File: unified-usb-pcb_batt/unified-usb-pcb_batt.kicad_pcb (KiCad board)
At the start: 2 copper layers, 30 x 34 mm, 39 parts, among them J1 QI, J2 USB_C_Receptacle_USB2.0, J3 USB_Out, J4 BATT, J5 THERM, SW1 SW_SPDT, U1 SRV05-4, U2 DW01A, U3 TP4056, U4 FS8205

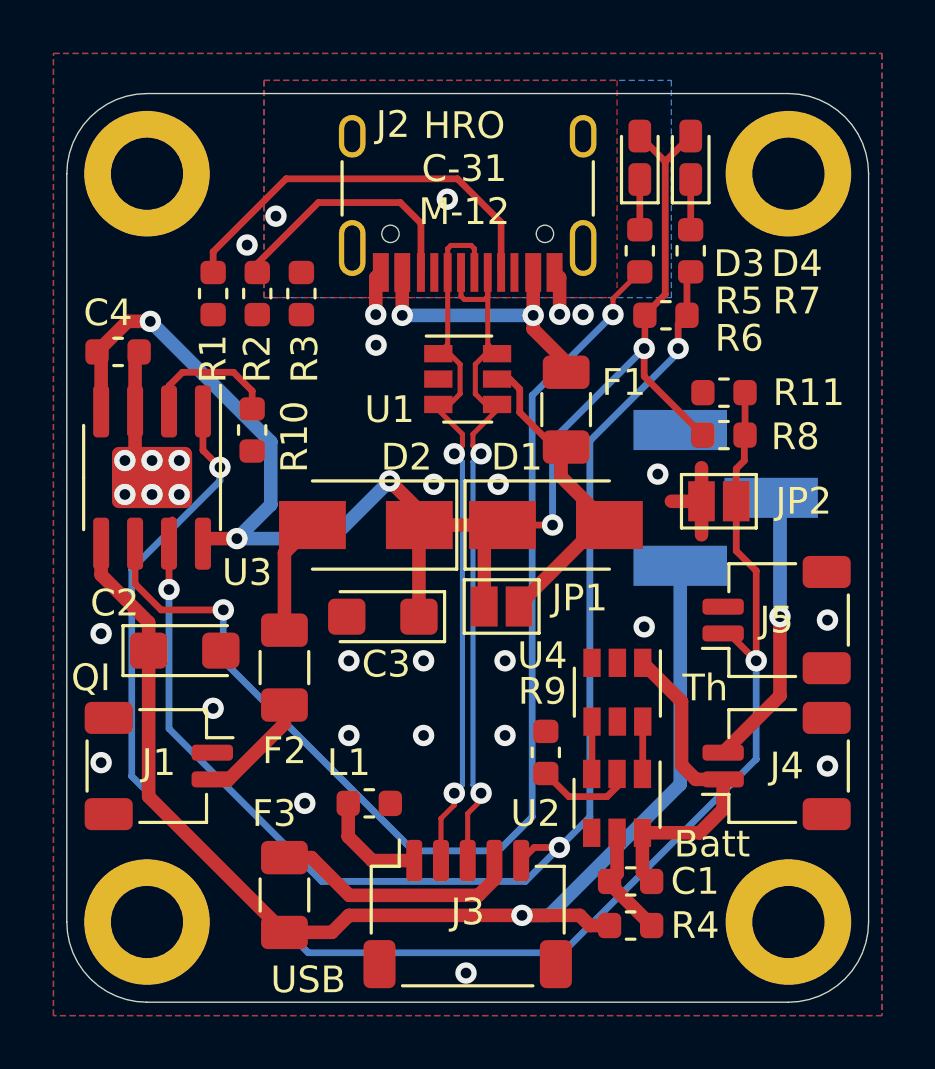
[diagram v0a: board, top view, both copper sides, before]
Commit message: fixed batt schem, added readme warning about broken pcb
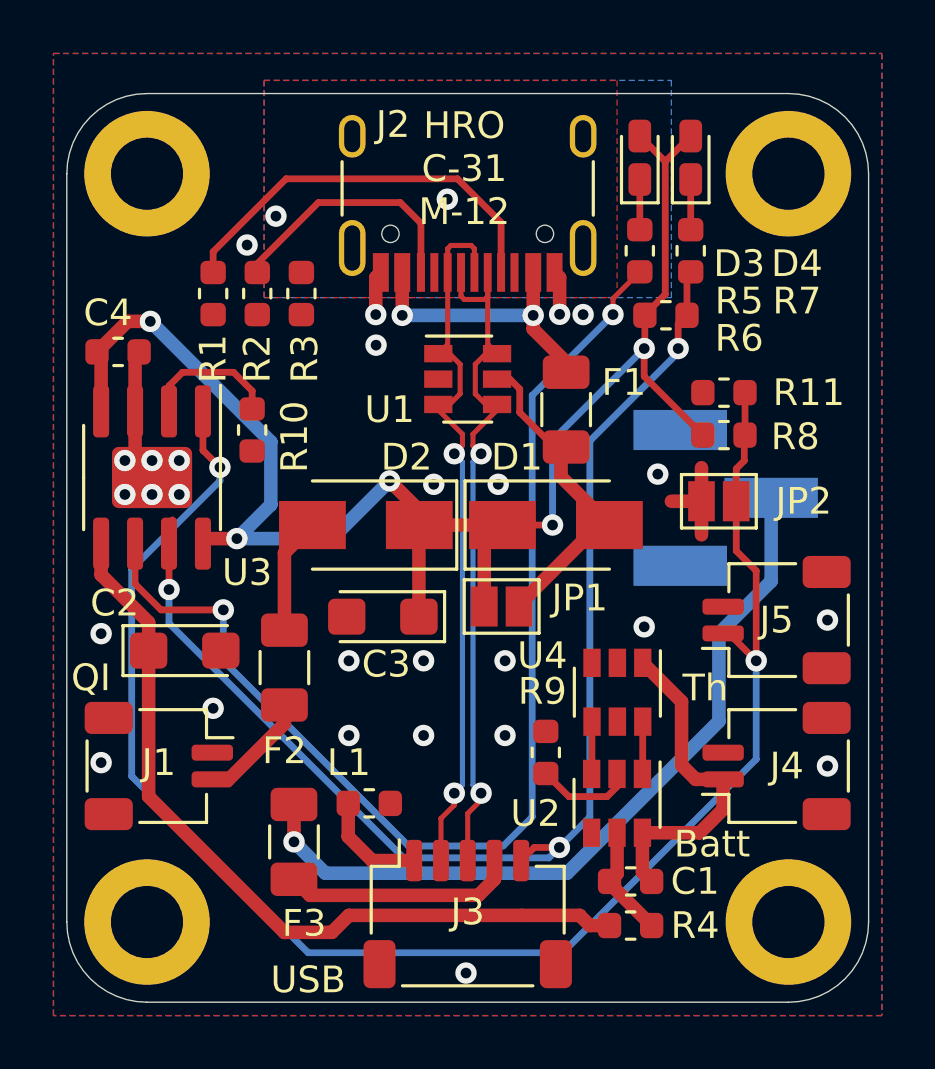
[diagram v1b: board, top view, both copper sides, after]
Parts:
- moved F3 2.02 mm to (24.3, 47.3), turned to 90 degrees
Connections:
- C2 pad 1: VOUT -> Net-(C2-Pad1)
- J4 pad 2: Net-(J4-Pad2) -> Net-(C2-Pad1)
- R4 pad 2: VOUT -> Net-(C2-Pad1)
- SW1 pad 1: Net-(SW1-Pad1) -> +5V
- SW1 pad 2: Net-(J4-Pad2) -> VOUT
- SW1 pad 3: VOUT -> Net-(C2-Pad1)
- U3 pad 5: VOUT -> Net-(C2-Pad1)
- U3 pad 9: GNDPWR -> (no net)
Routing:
- net Net-(C2-Pad1): track 0.00 -> 30.0 mm
- net VOUT: track 46.1 -> 30.0 mm
- net Net-(J4-Pad2): track 11.2 -> 0.00 mm, vias 1 -> 0
- net chgsense: track 49.7 -> 46.6 mm
- net Net-(F3-Pad1): track 9.39 -> 8.70 mm
- net GNDPWR: vias 28 -> 27

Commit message: slight rev bump - fixed battery pcb, re-exported new prod files for jlcpcb. Probably last commit, project no longer in active development
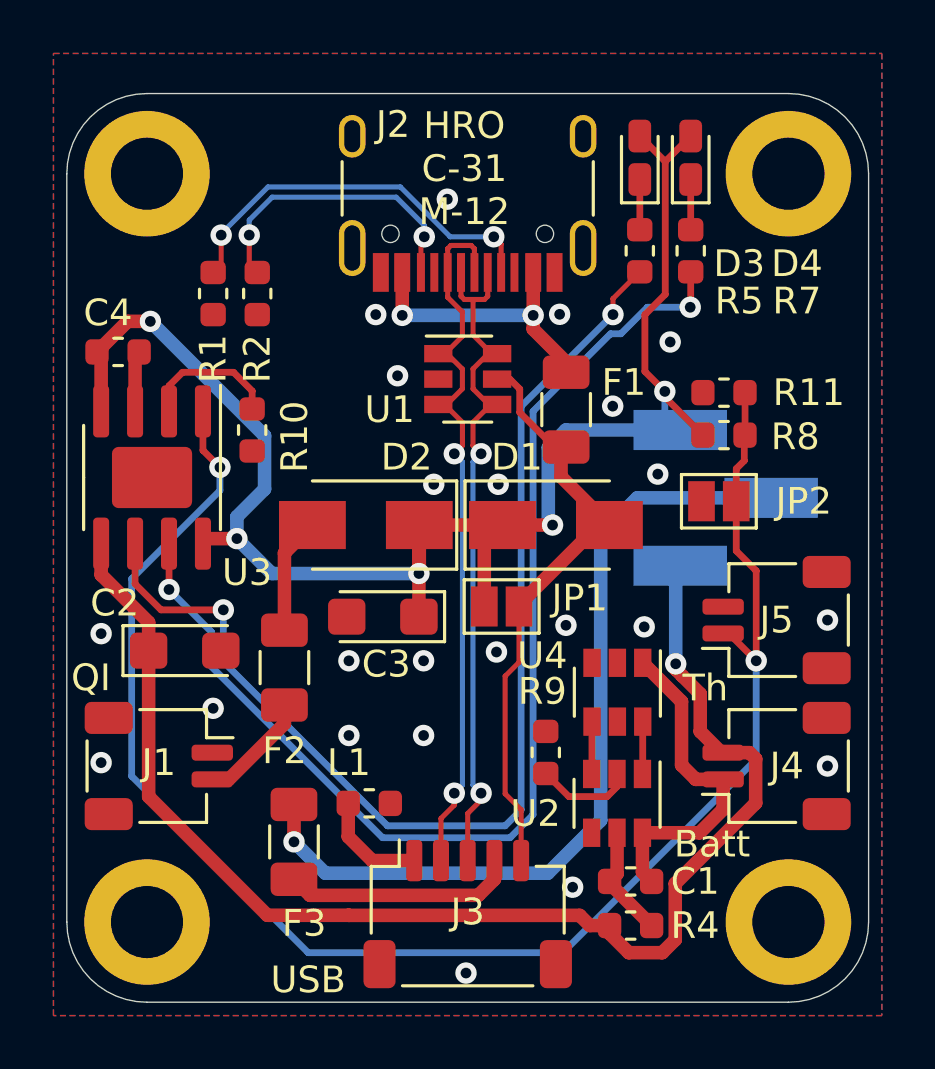
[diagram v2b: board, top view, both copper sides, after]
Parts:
- removed R3: 0, Resistor_SMD:R_0603_1608Metric
- removed R6: 10k, Resistor_SMD:R_0603_1608Metric
- D3: value 19-217/GHC-YR1S2/3T -> green
- D4: value KT-0603R -> orange
- moved H1 36.9 mm to (42.8, 50.3)
- moved H4 36.9 mm to (18.8, 22.3)
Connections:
- D1 pad 2: Net-(D1-Pad2) -> VBUS
- F1 pad 1: Net-(D1-Pad2) -> VBUS
- H1 pad 1: GNDPWR -> (no net)
- H2 pad 1: GNDPWR -> (no net)
- H3 pad 1: GNDPWR -> (no net)
- J1 pad MP: (no net) -> GNDPWR
- J2 pad A8: Net-(J2-PadA8) -> unconnected-(J2-PadA8)
- J2 pad B8: Net-(J2-PadB8) -> unconnected-(J2-PadB8)
- J2 pad S1: Net-(J2-PadS1) -> GNDPWR
- J3 pad 5: chgsense -> VBUS
- J3 pad MP: (no net) -> GNDPWR
- J4 pad MP: (no net) -> GNDPWR
- J5 pad MP: (no net) -> GNDPWR
- JP1 pad 2: Net-(D1-Pad2) -> VBUS
- R7 pad 1: chgsense -> Net-(R7-Pad1)
- U1 pad 5: Net-(D1-Pad2) -> VBUS
- U2 pad 4: Net-(U2-Pad4) -> unconnected-(U2-Pad4)
- U3 pad 7: chgsense -> Net-(R7-Pad1)
- U4 pad 2: Net-(U4-Pad2) -> unconnected-(U4-Pad2)
- U4 pad 5: Net-(U4-Pad5) -> unconnected-(U4-Pad5)
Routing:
- net chgsense: track 46.6 -> 0.00 mm, vias 3 -> 0
- net Net-(R7-Pad1): track 0.00 -> 44.2 mm, vias 0 -> 2
- net VBUS: track 0.00 -> 21.6 mm
- net Net-(C2-Pad1): track 30.0 -> 49.6 mm, vias 0 -> 1
- net Net-(D1-Pad2): track 12.5 -> 0.00 mm
- net GNDPWR: track 12.5 -> 2.07 mm, vias 27 -> 23
- net Net-(R5-Pad1): track 45.1 -> 43.1 mm
- net VOUT: track 30.0 -> 31.8 mm
- net USB_D-: track 27.2 -> 25.5 mm
- net Net-(J2-PadB5): track 9.52 -> 10.8 mm, vias 0 -> 2
- net Net-(J2-PadA5): track 15.2 -> 14.3 mm, vias 0 -> 2
- net Net-(J2-PadS1): vias 2 -> 0
- removed copper zone on B.Cu, net Net-(J2-PadS1)
- removed copper zone on F.Cu, net Net-(J2-PadS1)
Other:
- net class Default removed
- net class power removed
- board text added: "Type-C PCB [Li-Ion] rev 1.1 github.com/ebastler/unified-usb-pcb mpwr.xyz"
- board text removed: "Type-C PCB [Li-Ion] rev 1.0 github.com/ebastler/unified-usb-pcb mpwr.xyz"
